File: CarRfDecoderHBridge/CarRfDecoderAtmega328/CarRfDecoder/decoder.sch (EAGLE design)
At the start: 54 parts, among them U2 RFM69CW, U3 MCP73831, U4 ATMEGA328P, U6 MIC5219 3.3V, Y1 16MHZ

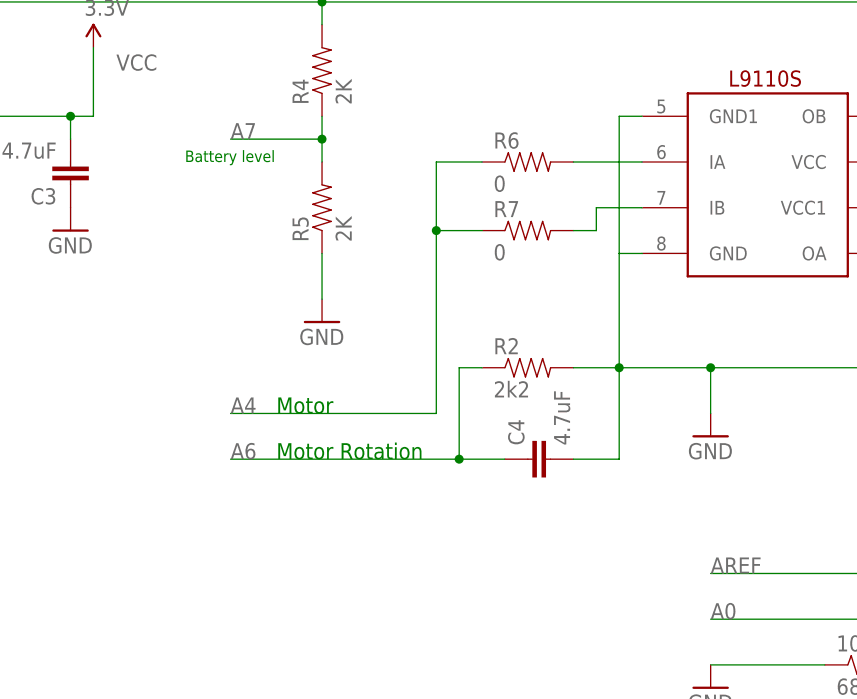
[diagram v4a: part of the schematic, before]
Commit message: Change the pin to H-bridge to allow reverse control of the motor using A5
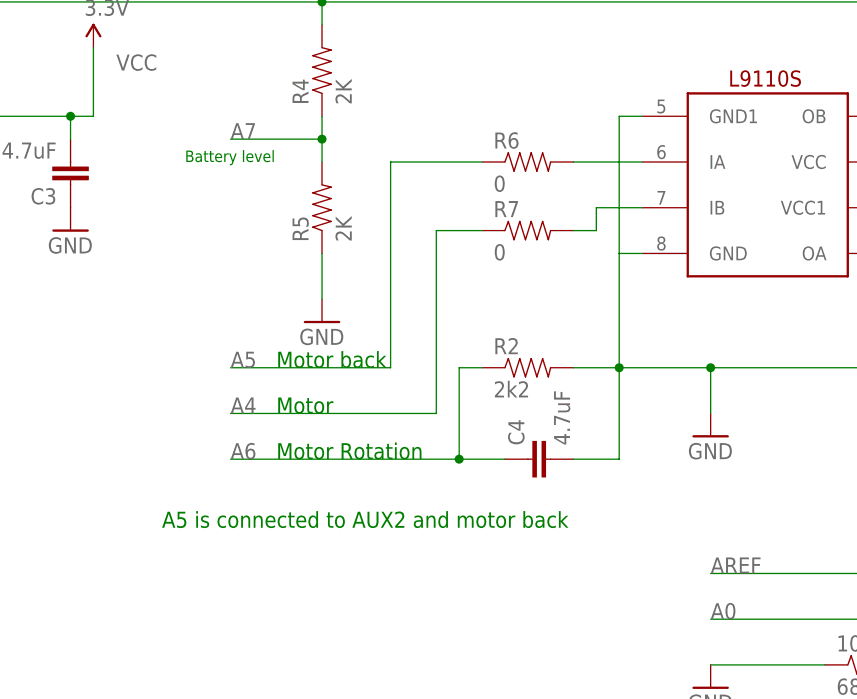
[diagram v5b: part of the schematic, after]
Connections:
- net A4: no longer R6.1
- net A5: now also R6.1
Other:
- note added: "A5 is connected to AUX2 and motor back"
- note added: "Motor back"
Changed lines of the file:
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@@
 <text x="124.46" y="86.36" size="1.778" layer="91">Motor</text>
 <text x="124.46" y="81.28" size="1.778" layer="91">Motor Rotation</text>
+<text x="124.46" y="91.44" size="1.778" layer="91">Motor back</text>
+<text x="111.76" y="73.66" size="1.778" layer="91">A5 is connected to AUX2 and motor back</text>
 </plain>
 <instances>
@@
 <label x="119.38" y="86.36" size="1.778" layer="95"/>
 <wire x1="142.24" y1="86.36" x2="142.24" y2="106.68" width="0.1524" layer="91"/>
-<pinref part="R6" gate="G$1" pin="1"/>
-<wire x1="142.24" y1="106.68" x2="142.24" y2="114.3" width="0.1524" layer="91"/>
-<wire x1="142.24" y1="114.3" x2="147.32" y2="114.3" width="0.1524" layer="91"/>
 <pinref part="R7" gate="G$1" pin="1"/>
 <wire x1="142.24" y1="106.68" x2="147.32" y2="106.68" width="0.1524" layer="91"/>
-<junction x="142.24" y="106.68"/>
 </segment>
 <segment>
@@
 <label x="172.72" y="-5.08" size="1.778" layer="95"/>
 </segment>
-</net>
+<segment>
+<pinref part="R6" gate="G$1" pin="1"/>
+<wire x1="147.32" y1="114.3" x2="137.16" y2="114.3" width="0.1524" layer="91"/>
+<wire x1="137.16" y1="114.3" x2="137.16" y2="91.44" width="0.1524" layer="91"/>
+<wire x1="137.16" y1="91.44" x2="119.38" y2="91.44" width="0.1524" layer="91"/>
+<label x="119.38" y="91.44" size="1.778" layer="95"/>
+</segment>
+</net>

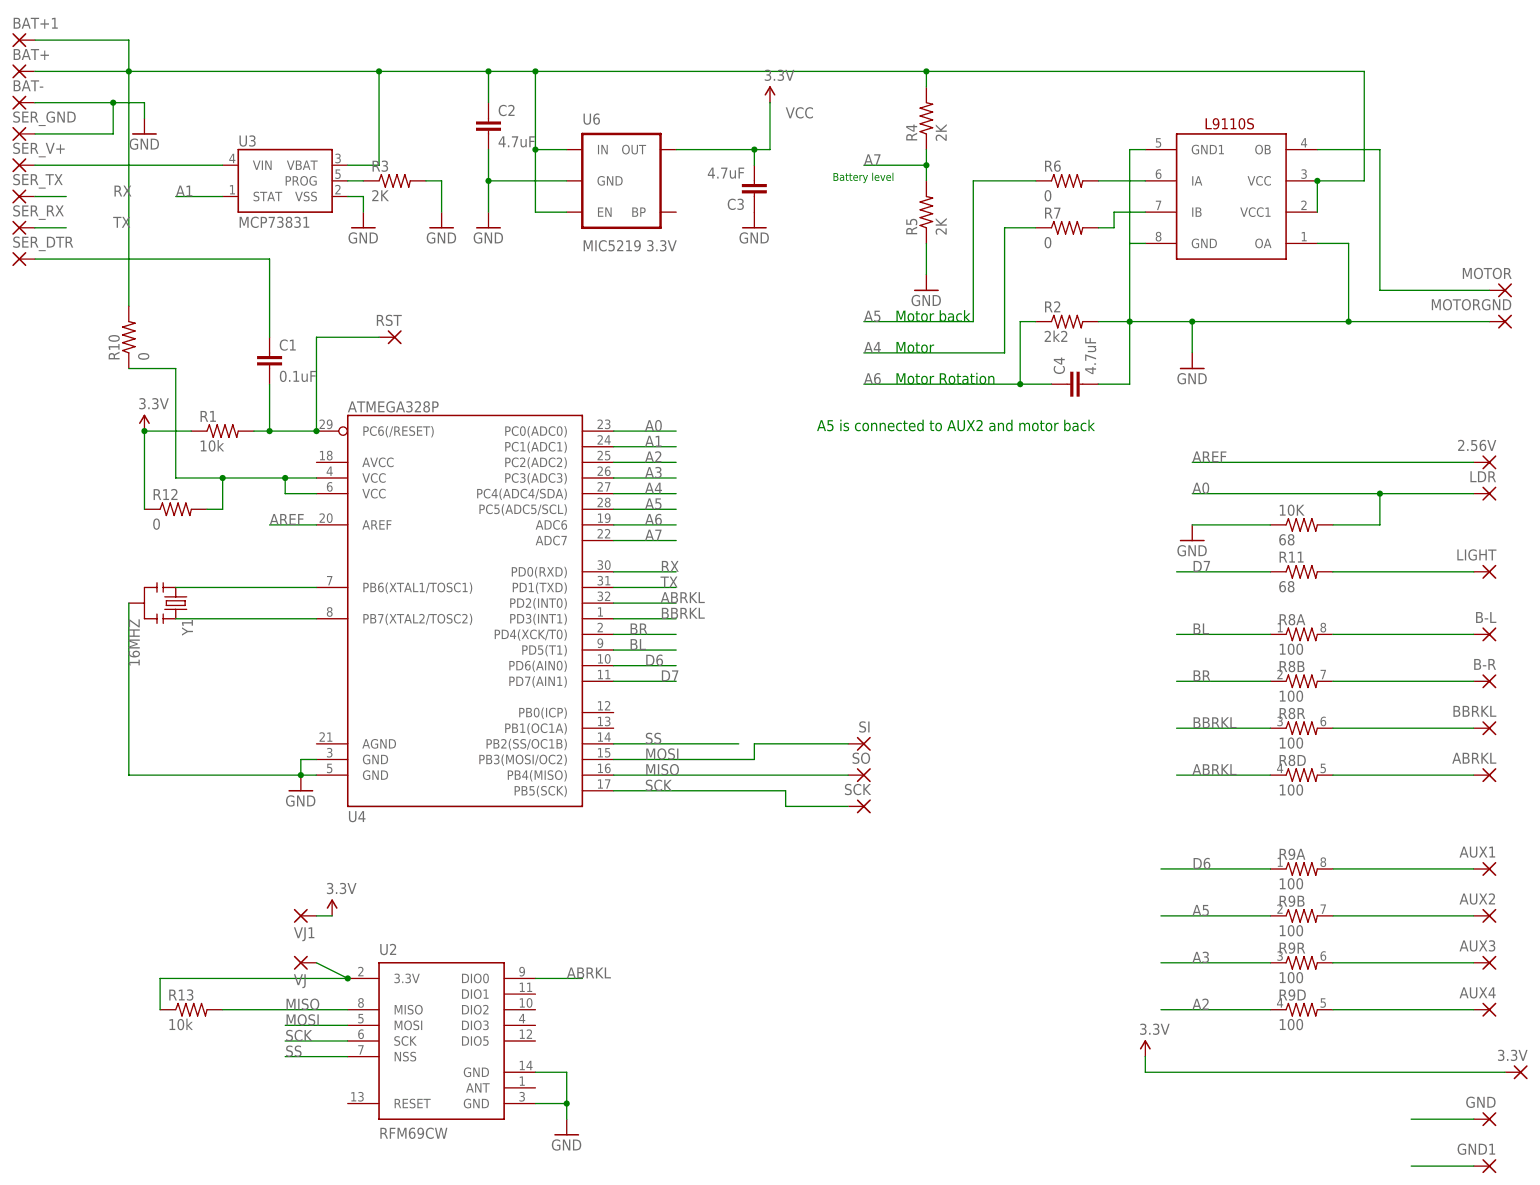
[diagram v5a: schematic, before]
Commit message: Fix R6 R7 bug. Disconnect motor from GND via R14
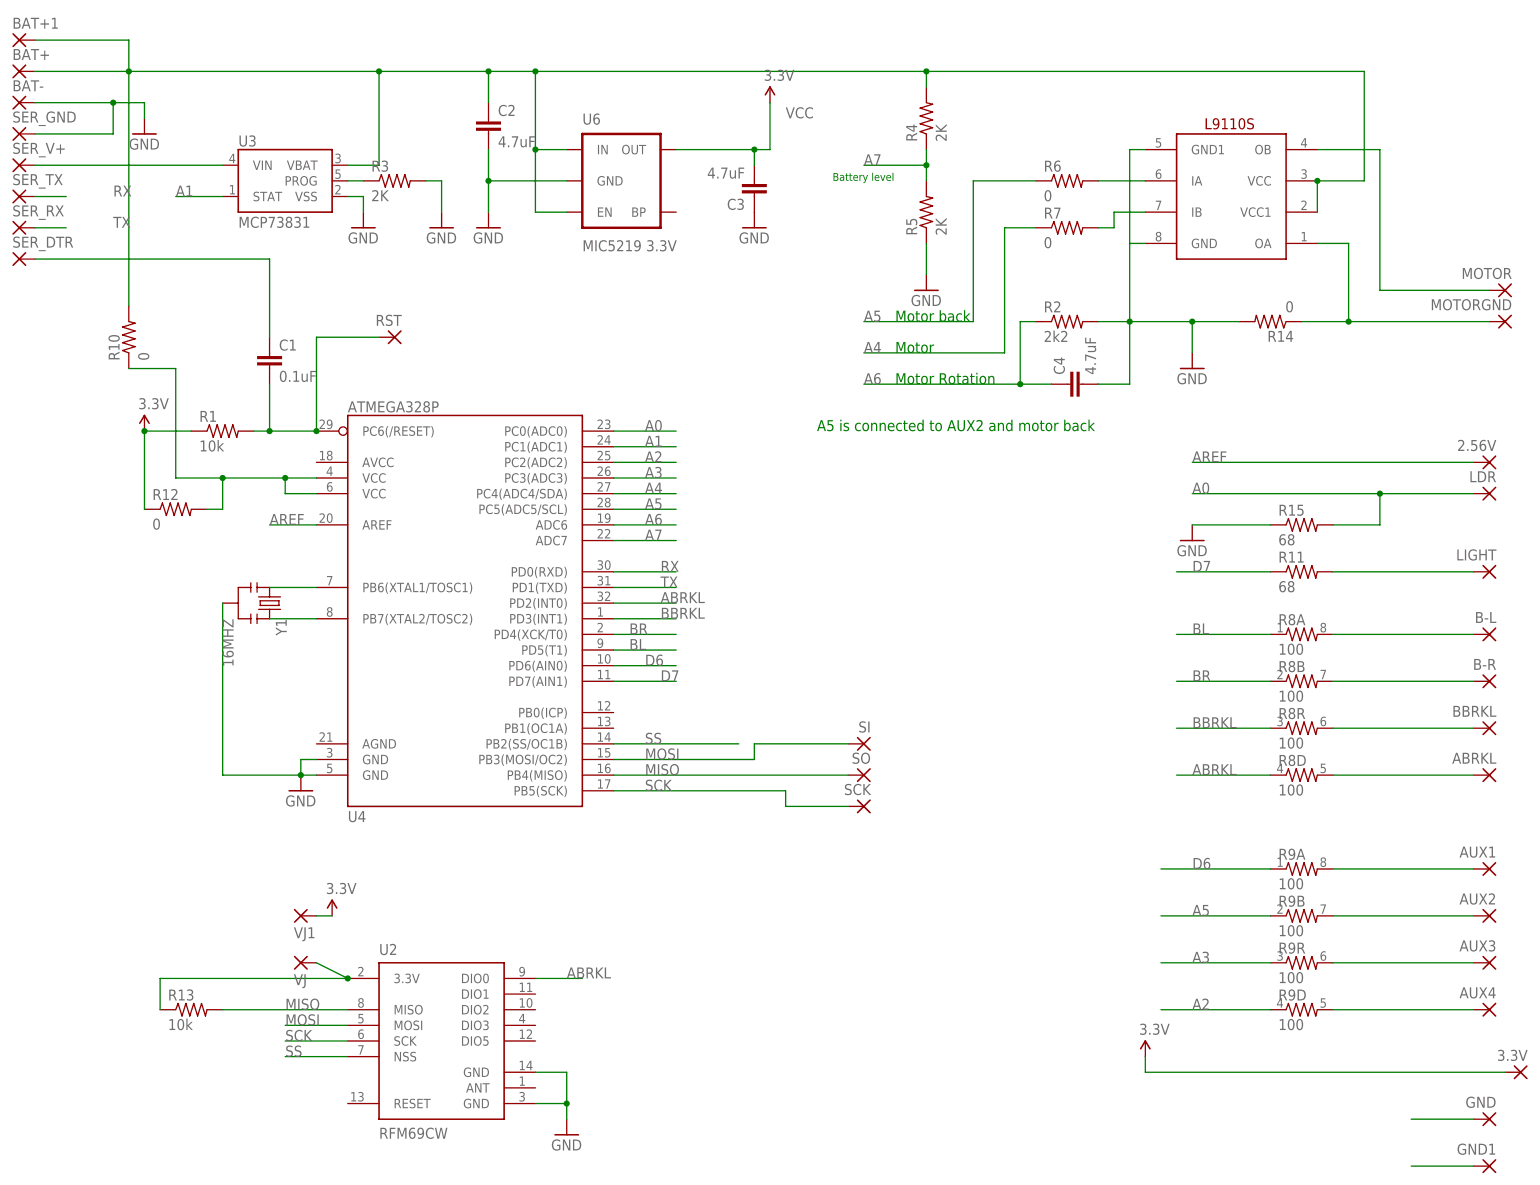
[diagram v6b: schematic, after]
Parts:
- added R14: 0, SparkFun-Resistors:RESISTOR0603-RES
- renumbered 10K to R15
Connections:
- new net OA: MDRIVER.OA, MOTORGND.P, R14.1
- net GND: now also R14.2; no longer MDRIVER.OA, MOTORGND.P
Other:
- moved on the sheet: Y1
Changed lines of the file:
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@@
 <part name="LIGHT" library="wirepad" deviceset="SMD2" device=""/>
 <part name="2.56V" library="wirepad" deviceset="SMD2" device=""/>
-<part name="10K" library="SparkFun-Resistors" deviceset="RESISTOR" device="0603-RES" value="68"/>
+<part name="R15" library="SparkFun-Resistors" deviceset="RESISTOR" device="0603-RES" value="68"/>
 <part name="LDR" library="wirepad" deviceset="SMD2" device=""/>
 <part name="GND11" library="SparkFun-Aesthetics" deviceset="GND" device=""/>
@@
 <part name="R13" library="SparkFun-Resistors" deviceset="RESISTOR" device="0603-RES" value="10k"/>
 <part name="BAT+1" library="wirepad" deviceset="SMD2" device=""/>
+<part name="R14" library="SparkFun-Resistors" deviceset="RESISTOR" device="0603-RES" value="0"/>
 </parts>
 <sheets>
@@
 <instance part="LIGHT" gate="1" x="220.98" y="50.8" rot="MR0"/>
 <instance part="2.56V" gate="1" x="220.98" y="68.58" rot="MR0"/>
-<instance part="10K" gate="G$1" x="190.5" y="58.42"/>
+<instance part="R15" gate="G$1" x="190.5" y="58.42"/>
 <instance part="LDR" gate="1" x="220.98" y="63.5" rot="MR0"/>
 <instance part="GND11" gate="1" x="172.72" y="55.88"/>
@@
 <instance part="VJ" gate="1" x="27.94" y="-12.7" rot="MR180"/>
 <instance part="VJ1" gate="1" x="27.94" y="-5.08" rot="MR180"/>
-<instance part="Y1" gate="G$1" x="7.62" y="45.72" rot="R270"/>
+<instance part="Y1" gate="G$1" x="22.86" y="45.72" rot="R270"/>
 <instance part="GND" gate="1" x="220.98" y="-38.1" rot="MR0"/>
 <instance part="GND1" gate="1" x="220.98" y="-45.72" rot="MR0"/>
@@
 <instance part="R13" gate="G$1" x="10.16" y="-20.32"/>
 <instance part="BAT+1" gate="1" x="-17.78" y="137.16"/>
+<instance part="R14" gate="G$1" x="185.42" y="91.44" rot="R180"/>
 </instances>
 <busses>
@@
 <wire x1="172.72" y1="86.36" x2="172.72" y2="91.44" width="0.1524" layer="91"/>
 <junction x="172.72" y="91.44"/>
-<wire x1="172.72" y1="91.44" x2="198.12" y2="91.44" width="0.1524" layer="91"/>
-<pinref part="MOTORGND" gate="1" pin="P"/>
-<pinref part="MDRIVER" gate="G$1" pin="OA"/>
-<wire x1="198.12" y1="91.44" x2="220.98" y2="91.44" width="0.1524" layer="91"/>
-<wire x1="193.04" y1="104.14" x2="198.12" y2="104.14" width="0.1524" layer="91"/>
-<wire x1="198.12" y1="104.14" x2="198.12" y2="91.44" width="0.1524" layer="91"/>
-<junction x="198.12" y="91.44"/>
+<wire x1="172.72" y1="91.44" x2="180.34" y2="91.44" width="0.1524" layer="91"/>
 <pinref part="MDRIVER" gate="G$1" pin="GND1"/>
 <wire x1="165.1" y1="119.38" x2="162.56" y2="119.38" width="0.1524" layer="91"/>
@@
 <wire x1="162.56" y1="104.14" x2="162.56" y2="91.44" width="0.1524" layer="91"/>
 <pinref part="R2" gate="G$1" pin="2"/>
-</segment>
-<segment>
-<pinref part="10K" gate="G$1" pin="1"/>
+<pinref part="R14" gate="G$1" pin="2"/>
+</segment>
+<segment>
+<pinref part="R15" gate="G$1" pin="1"/>
 <wire x1="185.42" y1="58.42" x2="172.72" y2="58.42" width="0.1524" layer="91"/>
 <pinref part="GND11" gate="1" pin="GND"/>
@@
 <junction x="27.94" y="17.78"/>
 <pinref part="Y1" gate="G$1" pin="2"/>
-<wire x1="0" y1="17.78" x2="27.94" y2="17.78" width="0.1524" layer="91"/>
-<wire x1="0" y1="45.72" x2="0" y2="17.78" width="0.1524" layer="91"/>
+<wire x1="15.24" y1="17.78" x2="27.94" y2="17.78" width="0.1524" layer="91"/>
+<wire x1="15.24" y1="45.72" x2="15.24" y2="17.78" width="0.1524" layer="91"/>
 </segment>
 <segment>
@@
 <pinref part="LDR" gate="1" pin="P"/>
 <wire x1="218.44" y1="63.5" x2="203.2" y2="63.5" width="0.1524" layer="91"/>
-<pinref part="10K" gate="G$1" pin="2"/>
+<pinref part="R15" gate="G$1" pin="2"/>
 <wire x1="203.2" y1="63.5" x2="172.72" y2="63.5" width="0.1524" layer="91"/>
 <wire x1="195.58" y1="58.42" x2="203.2" y2="58.42" width="0.1524" layer="91"/>
@@
 <segment>
 <pinref part="U4" gate="G$1" pin="PB6(XTAL1/TOSC1)"/>
-<wire x1="7.62" y1="48.26" x2="30.48" y2="48.26" width="0.1524" layer="91"/>
+<wire x1="22.86" y1="48.26" x2="30.48" y2="48.26" width="0.1524" layer="91"/>
 <pinref part="Y1" gate="G$1" pin="1"/>
 </segment>
@@
 <segment>
 <pinref part="U4" gate="G$1" pin="PB7(XTAL2/TOSC2)"/>
-<wire x1="7.62" y1="43.18" x2="30.48" y2="43.18" width="0.1524" layer="91"/>
+<wire x1="22.86" y1="43.18" x2="30.48" y2="43.18" width="0.1524" layer="91"/>
 <pinref part="Y1" gate="G$1" pin="3"/>
 </segment>
@@
 </segment>
 </net>
+<net name="OA" class="0">
+<segment>
+<pinref part="MOTORGND" gate="1" pin="P"/>
+<wire x1="198.12" y1="91.44" x2="220.98" y2="91.44" width="0.1524" layer="91"/>
+<pinref part="MDRIVER" gate="G$1" pin="OA"/>
+<wire x1="193.04" y1="104.14" x2="198.12" y2="104.14" width="0.1524" layer="91"/>
+<wire x1="198.12" y1="104.14" x2="198.12" y2="91.44" width="0.1524" layer="91"/>
+<junction x="198.12" y="91.44"/>
+<wire x1="190.5" y1="91.44" x2="198.12" y2="91.44" width="0.1524" layer="91"/>
+<pinref part="R14" gate="G$1" pin="1"/>
+</segment>
+</net>
